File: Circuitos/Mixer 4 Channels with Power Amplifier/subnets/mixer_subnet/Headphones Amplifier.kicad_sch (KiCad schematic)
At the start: 12 parts

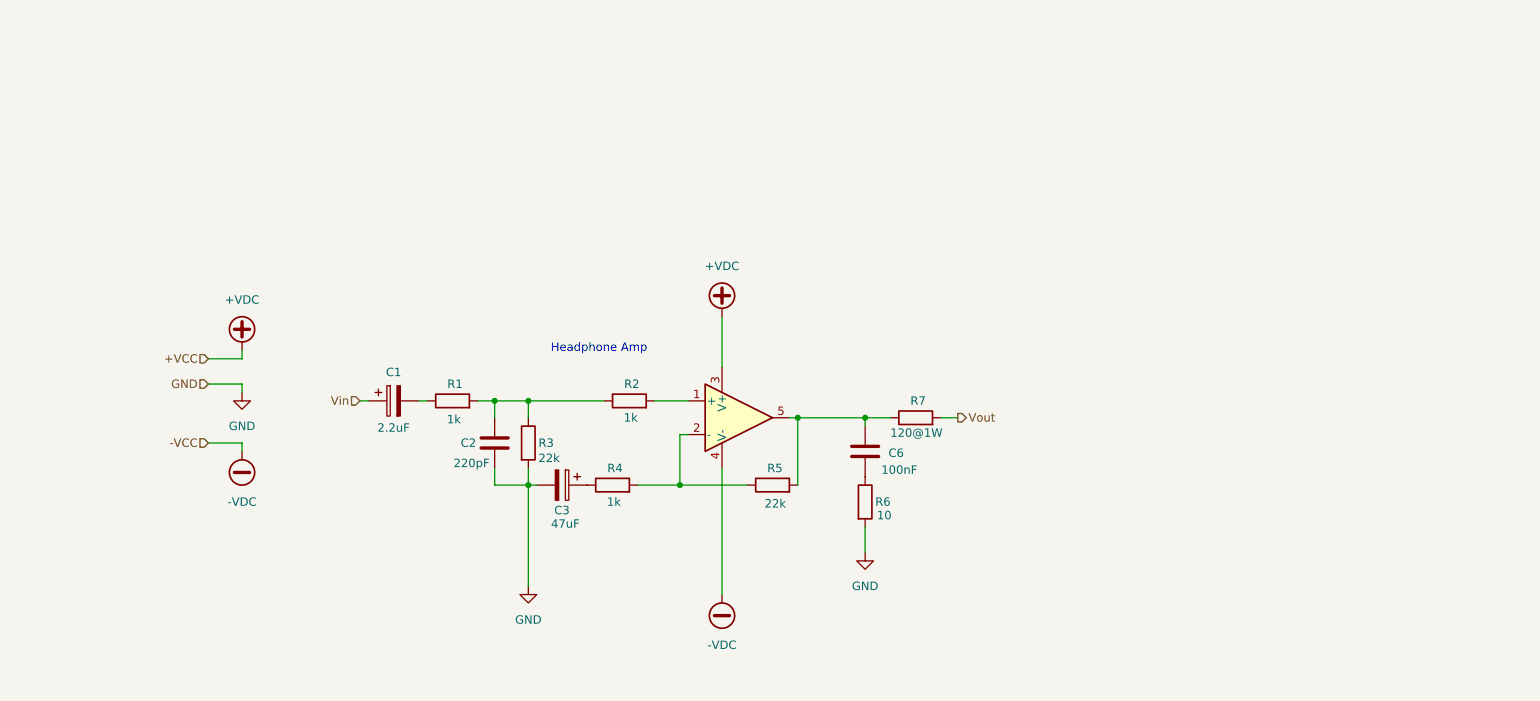
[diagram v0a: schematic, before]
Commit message: Correcciones y modificaciones en fuente, amp auriculares y simul completa
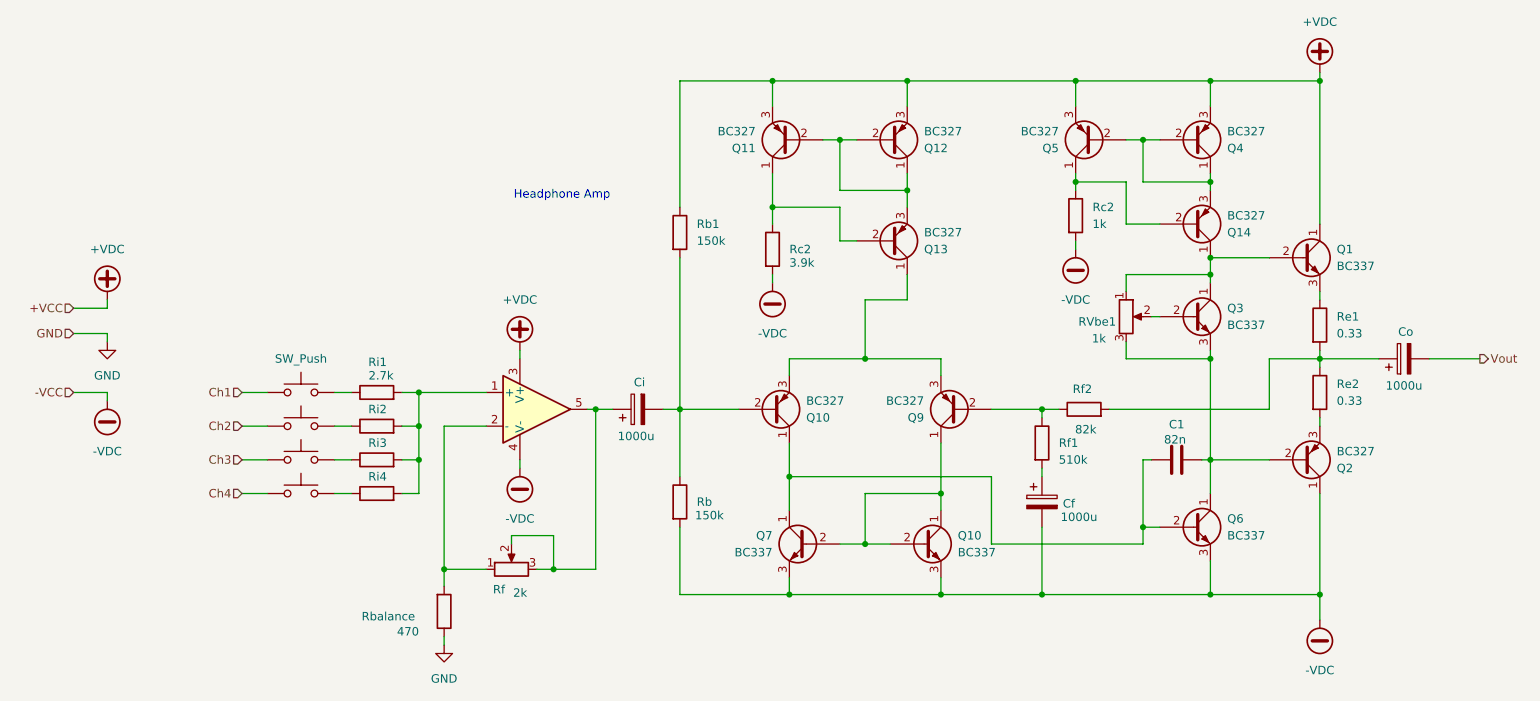
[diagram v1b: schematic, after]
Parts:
- removed C1: 2.2uF, symbol Device:C_Polarized
- removed C2: 220pF, symbol Device:C
- removed C3: 47uF, symbol Device:C_Polarized
- removed C6: 100nF, symbol Device:C
- removed R1, R2, R4: 1k, symbol Device:R
- removed R3, R5: 22k, symbol Device:R
- removed R6: 10, symbol Device:R
- removed R7: 120@1W, symbol Device:R
- removed U?: ${SIM.PARAMS}, symbol Simulation_SPICE:OPAMP
- added C1: 82n, symbol Device:C
- added Cf, Ci, Co: 1000u, symbol Device:C_Polarized
- added Q1, Q10, Q3, Q6, Q7: BC337, Package_TO_SOT_THT:TO-92_Inline, symbol Transistor_BJT:BC337
- added Q10, Q11, Q12, Q13, Q14, Q2, Q4, Q5, Q9: BC327, Package_TO_SOT_THT:TO-92_Inline, symbol Transistor_BJT:BC327
- added RVbe1: 1k, symbol Device:R_Potentiometer
- added Rb, Rb1: 150k, symbol Device:R
- added Rbalance: 470, symbol Device:R
- added Rc2: 1k, symbol Device:R
- added Rc2: 3.9k, symbol Device:R
- added Re1, Re2: 0.33, symbol Device:R
- added Rf: 2k, symbol Device:R_Potentiometer
- added Rf1: 510k, symbol Device:R
- added Rf2: 82k, symbol Device:R
- added Ri1, Ri2, Ri3, Ri4: 2.7k, symbol Device:R
- added SW4, SW5, SW6, SW7: SW_Push, symbol Switch:SW_Push
- added U6: ${SIM.PARAMS}, symbol Simulation_SPICE:OPAMP
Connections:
- net +VDC: now also Q1.1 (C), Q11.3 (E), Q12.3 (E), Q4.3 (E), Q5.3 (E), Rb1.1, U6.3 (V+)
- net -VDC: now also Cf.2, Q10.3 (E), Q2.1 (C), Q6.3 (E), Q7.3 (E), Rb.2, Rc2.2, Rc2.2, U6.4 (V-)
- net GND: now also Rbalance.1
- net Vout: now also Co.2
- new net: Q10.1 (C), Q10.2 (B), Q7.2 (B), Q9.1 (C)
- new net: C1.1, Q10.1 (C), Q6.2 (B), Q7.1 (C)
- new net: C1.2, Q2.2 (B), Q3.3 (E), Q6.1 (C), RVbe1.3
- new net: Q14.2 (B), Q5.1 (C), Rc2.1
- new net: Rbalance.2, Rf.1, U6.2 (-)
- new net: Ci.1, Rf.2, Rf.3, U6.5
- new net: Ri4.1, SW7.2
- new net: Ri1.2, Ri2.2, Ri3.2, Ri4.2, U6.1 (+)
- new net: Q2.3 (E), Re2.2
- new net: Co.1, Re1.2, Re2.1, Rf2.2
- new net: Ri2.1, SW5.2
- new net: Ci.2, Q10.2 (B), Rb.1, Rb1.2
- new net: Q11.1 (C), Q13.2 (B), Rc2.1
- new net: Q9.2 (B), Rf1.1, Rf2.1
- new net: Cf.1, Rf1.2
- new net: Ri3.1, SW6.2
- new net: Q1.2 (B), Q14.1 (C), Q3.1 (C), RVbe1.1
- new net: Q1.3 (E), Re1.1
- new net: Q11.2 (B), Q12.1 (C), Q12.2 (B), Q13.3 (E)
- new net: Q14.3 (E), Q4.1 (C), Q4.2 (B), Q5.2 (B)
- new net: Ri1.1, SW4.2
- new net: Q10.3 (E), Q13.1 (C), Q9.3 (E)
- new net: Q3.2 (B), RVbe1.2
- new net Ch1: SW4.1
- new net Ch2: SW5.1
- new net Ch3: SW6.1
- new net Ch4: SW7.1

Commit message: Informe finalizado
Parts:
- Cf: value 1000u -> 100u
- Rc1: renamed from Rc2; value 1k -> 680
- Rc2: value 3.9k -> 2.7k
- renumbered C1 to CM, Q10 to Q11, Q11 to Q14, Q14 to Q7, Q7 to Q8
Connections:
- net -VDC is gone; now on net GND: Cf.2, Q11.3 (E), Q2.1 (C), Q6.3 (E), Q8.3 (E), Rb.2, Rc1.2, Rc2.2, U6.4 (V-)
- net +VDC renamed +VDC2

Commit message: Final de proyecto
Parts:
- removed Cf: 100u, symbol Device:C_Polarized
- added Cf: 15n, symbol Device:C
- CM: value 82n -> 47n
- Ci: value 1000u -> 1u
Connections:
- net GND: now also Cf.1
- net at Rf1.2: now also Cf.2
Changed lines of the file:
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@@
+	)
+	(symbol
+		(lib_id "Device:C")
+		(at 184.15 116.84 180)
+		(unit 1)
+		(exclude_from_sim no)
+		(in_bom yes)
+		(on_board yes)
+		(dnp no)
+		(property "Reference" "Cf"
+			(at 188.722 115.316 0)
+			(effects
+				(font
+					(size 1.27 1.27)
+				)
+			)
+		)
+		(property "Value" "15n"
+			(at 189.23 117.856 0)
+			(effects
+				(font
+					(size 1.27 1.27)
+				)
+			)
+		)
+		(property "Footprint" ""
+			(at 183.1848 113.03 0)
+			(effects
+				(font
+					(size 1.27 1.27)
+				)
+				(hide yes)
+			)
+		)
+		(property "Datasheet" "~"
+			(at 184.15 116.84 0)
+			(effects
+				(font
+					(size 1.27 1.27)
+				)
+				(hide yes)
+			)
+		)
+		(property "Description" "Unpolarized capacitor"
+			(at 184.15 116.84 0)
+			(effects
+				(font
+					(size 1.27 1.27)
+				)
+				(hide yes)
+			)
+		)
+		(pin "2"
+		)
+		(pin "1"
+		)
+		(instances
+			(project "Mixer 4 Channels with Power Amplifier"
+				(path "/0e2446e7-fd41-47c0-87b8-110c51786f7b/7f4f2712-287c-4d36-933e-3ea06b7ca144/2120dfdf-fe8b-445e-ae2f-50e2c5d036a2"
+					(reference "Cf")
+					(unit 1)
+				)
+			)
+		)
 	)
 	(symbol
@@
 			)
 		)
-		(property "Value" "82n"
+		(property "Value" "47n"
 			(at 204.216 107.442 90)
 			(effects
@@
 	)
 	(symbol
-		(lib_id "Device:C_Polarized")
-		(at 184.15 116.84 0)
-		(unit 1)
-		(exclude_from_sim no)
-		(in_bom yes)
-		(on_board yes)
-		(dnp no)
-		(property "Reference" "Cf"
-			(at 188.214 117.094 0)
-			(effects
-				(font
-					(size 1.27 1.27)
-				)
-			)
-		)
-		(property "Value" "100u"
-			(at 189.738 119.126 0)
-			(effects
-				(font
-					(size 1.27 1.27)
-				)
-			)
-		)
-		(property "Footprint" ""
-			(at 185.1152 120.65 0)
-			(effects
-				(font
-					(size 1.27 1.27)
-				)
-				(hide yes)
-			)
-		)
-		(property "Datasheet" "~"
-			(at 184.15 116.84 0)
-			(effects
-				(font
-					(size 1.27 1.27)
-				)
-				(hide yes)
-			)
-		)
-		(property "Description" "Polarized capacitor"
-			(at 184.15 116.84 0)
-			(effects
-				(font
-					(size 1.27 1.27)
-				)
-				(hide yes)
-			)
-		)
-		(pin "1"
-		)
-		(pin "2"
-		)
-		(instances
-			(project "Mixer 4 Channels with Power Amplifier"
-				(path "/0e2446e7-fd41-47c0-87b8-110c51786f7b/7f4f2712-287c-4d36-933e-3ea06b7ca144/2120dfdf-fe8b-445e-ae2f-50e2c5d036a2"
-					(reference "Cf")
-					(unit 1)
-				)
-			)
-		)
-	)
-	(symbol
 		(lib_id "Switch:SW_Push")
 		(at 72.39 100.33 0)
@@
 			)
 		)
-		(property "Value" "1000u"
+		(property "Value" "1u"
 			(at 122.936 106.934 90)
 			(effects
